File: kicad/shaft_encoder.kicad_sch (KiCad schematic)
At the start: 0 parts

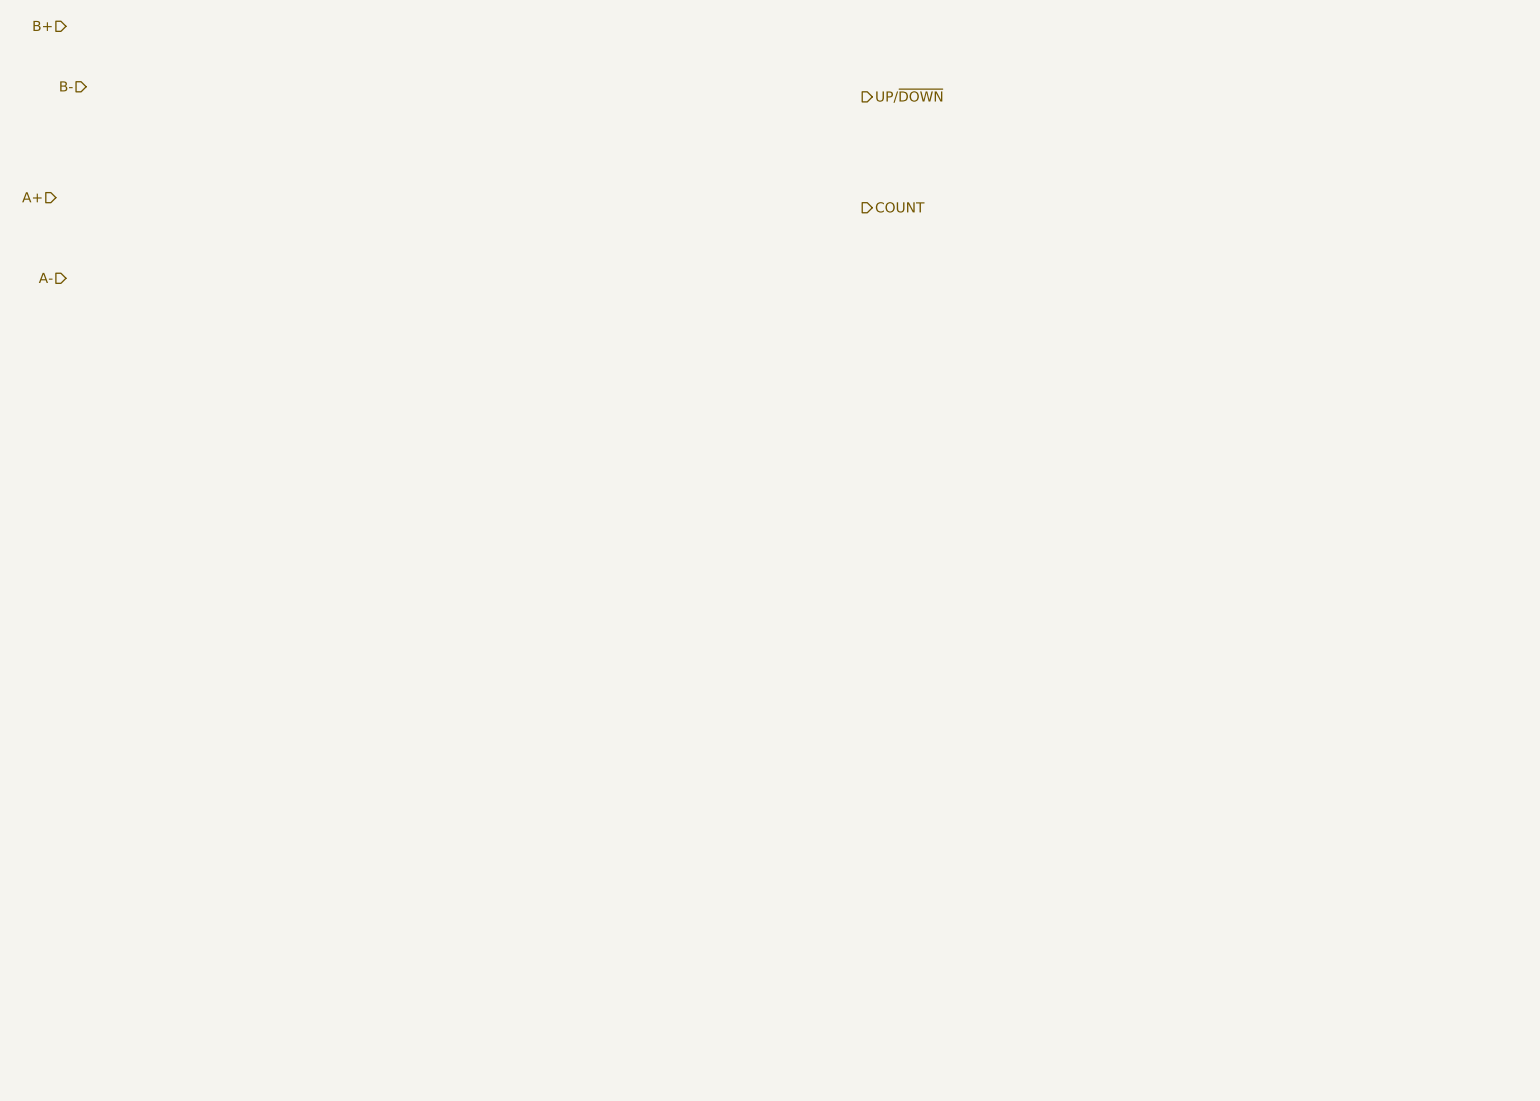
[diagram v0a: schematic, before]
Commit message: Completed the schematic. All components have Digikey part numbers and footprints. The power supply sheet still requires some work.
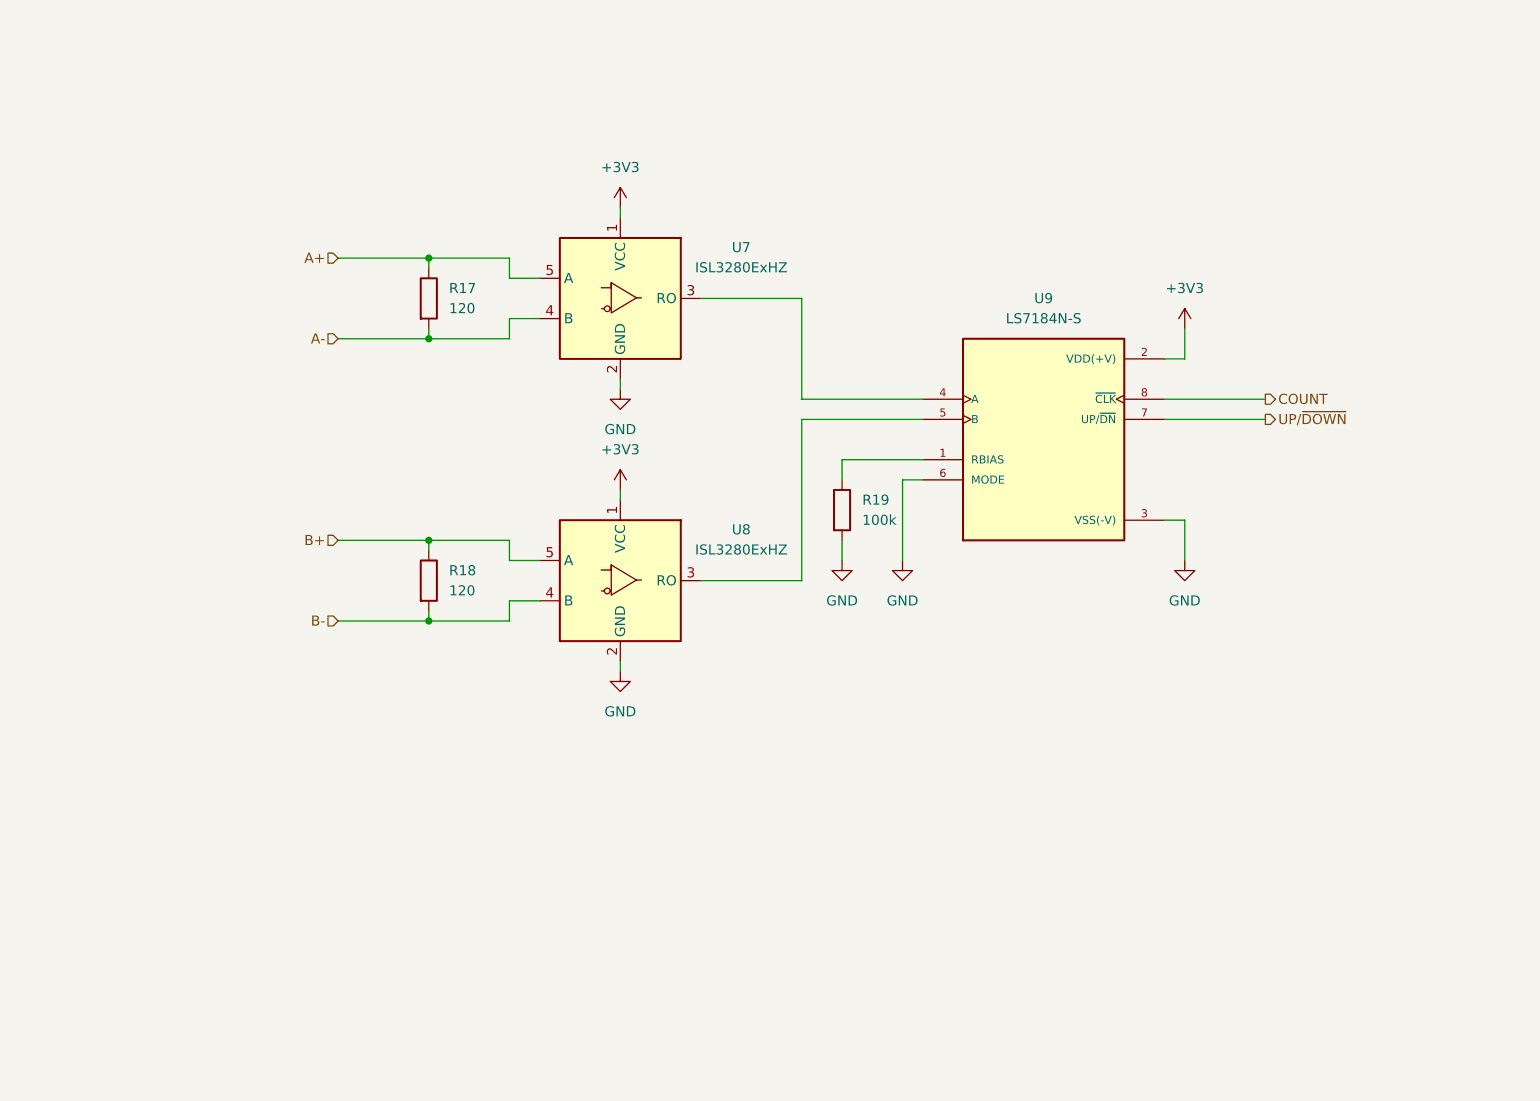
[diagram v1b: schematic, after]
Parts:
- added R17, R18: 120, Resistor_SMD:R_0603_1608Metric, symbol Device:R
- added R19: 100k, Resistor_SMD:R_0603_1608Metric, symbol Device:R
- added U7, U8: ISL3280ExHZ, Package_TO_SOT_SMD:SOT-23-5, symbol Interface_UART:ISL3280ExHZ
- added U9: LS7184N-S, local_library:SOIC127P600X175-8N, symbol local_library:LS7184N-S
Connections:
- net A+: now also R17.1, U7.5 (A)
- net A-: now also R17.2, U7.4 (B)
- net B+: now also R18.1, U8.5 (A)
- net B-: now also R18.2, U8.4 (B)
- net COUNT: now also U9.8 (~{CLK})
- net UP/~{DOWN}: now also U9.7 (UP/~{DN})
- new net: U7.3 (RO), U9.4 (A)
- new net: R19.1, U9.1 (RBIAS)
- new net: U8.3 (RO), U9.5 (B)
- new net +3V3: U7.1 (VCC), U8.1 (VCC), U9.2 (VDD(+V))
- new net GND: R19.2, U7.2 (GND), U8.2 (GND), U9.3 (VSS(-V)), U9.6 (MODE)
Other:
- company: (none) -> NX Solutions
- title: (none) -> TV slider

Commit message: Updated all schematic pages except the power supply. Did the initial component placement.
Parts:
- added C31, C32: 100p, Capacitor_SMD:C_0603_1608Metric, symbol Device:C
- added C33: 10u, Capacitor_SMD:C_0805_2012Metric, symbol Device:C
- added C34, C35, C36, C37: 100n, Capacitor_SMD:C_0603_1608Metric, symbol Device:C
- added D6, D7: SM712_SOT23, Package_TO_SOT_SMD:SOT-23, symbol Diode:SM712_SOT23
- added D8: SMF6V0A, Diode_SMD:D_SMF, symbol Diode:SMF6V0A
- added F2: 0.2A, Fuse:Fuse_1206_3216Metric, symbol Device:Polyfuse
- added FB5: BLM21PG221SN1D, Inductor_SMD:L_0805_2012Metric, symbol Device:FerriteBead
- added R18, R20, R21, R24: 10, Resistor_SMD:R_0603_1608Metric, symbol Device:R
- R19: renamed from R17; SupplierPN RC0603FR-07120RL -> 311-120HRCT-ND
- renumbered R19 to R22, R18 to R23, U9 to U8, U8 to U9
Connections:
- net +3V3: now also C35.1, C36.1, C37.1
- net A+: now also D6.2 (A2), R18.1; no longer R19.1, U7.5 (A)
- net A-: now also D6.1 (A1), R20.1; no longer R19.2, U7.4 (B)
- net B+: now also D7.2 (A2), R21.1; no longer R23.1, U9.5 (A)
- net B-: now also D7.1 (A1), R24.1; no longer R23.2, U9.4 (B)
- net GND: now also C33.2, C34.2, C35.2, C36.2, C37.2, D6.3 (common), D7.3 (common), D8.2 (A2)
- new net: C31.2, R19.2, R20.2, U7.4 (B)
- new net: C31.1, R18.2, R19.1, U7.5 (A)
- new net: C32.2, R23.2, R24.2, U9.4 (B)
- new net: C32.1, R21.2, R23.1, U9.5 (A)
- new net: F2.1, FB5.2
- new net +5V: F2.2
- new net +5Vout: C33.1, C34.1, D8.1 (A1), FB5.1
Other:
- moved on the sheet: R19, R22, R23, U7, U8, U9

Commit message: Finished the schematic and started the PCB.
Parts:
- R19: renamed from R22; SupplierPN RC0603FR-07100KL -> 311-100KHRCT-ND
- renumbered R18 to R15, R19 to R16, R20 to R17, R21 to R18, R23 to R20, R24 to R21, U7 to U6, U8 to U7, U9 to U8

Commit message: Reviewed the part numbers, footprints and pin numbers.
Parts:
- C31, C32: Dielectric X7R -> C0G, NP0
- C33: MP GRM21BR61E106KA73K -> GRM21BR61H106KE43L; SupplierPN 490-16824-1-ND -> 490-18663-1-ND; Voltage 25V -> 50V
- D6, D7: MF (none) -> SMC Diode Solutions; MP (none) -> SM712; Supplier (none) -> Digi-Key; SupplierPN (none) -> 1655-SM712CT-ND
- D8: MF (none) -> Vishay; MP (none) -> SMF6V0A-E3-08; Supplier (none) -> Digi-Key; SupplierPN (none) -> SMF6V0A-E3-08CT-ND; Voltage (none) -> 10.3V
- F2: value 0.2A -> 200mA
- R20: SupplierPN RC0603FR-07120RL -> 311-120HRCT-ND

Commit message: Removed DNP for shaft encoder filtering
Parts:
- C31, C32: now fitted
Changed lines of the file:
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@@
 		(in_bom yes)
 		(on_board yes)
-		(dnp yes)
+		(dnp no)
 		(fields_autoplaced yes)
 		(property "Reference" "C32"
@@
 		(in_bom yes)
 		(on_board yes)
-		(dnp yes)
+		(dnp no)
 		(fields_autoplaced yes)
 		(property "Reference" "C31"

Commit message: Re-annotated and added extra capacitors for the 5V and 3V3 DC-DC converters. Added testpoints to the electronic fuse.
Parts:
- renumbered C31 to C33, C32 to C34, C33 to C35, C34 to C36, C35 to C37, C36 to C38, C37 to C39, R15 to R16, R16 to R17, R17 to R18, R18 to R19, R19 to R20, R20 to R21, R21 to R22
